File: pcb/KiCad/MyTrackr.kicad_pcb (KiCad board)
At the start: 2 copper layers, 50 x 50 mm, 37 parts, among them CN1 ANT, CON1 MICRO_SD, P1 OLED, P2 ICSP, P3 CONN_01X05, P4 CONN_BAT, Q1 Q_PMOS_GSD, SW1 RESET, SW2 SEL, SW3 NEXT, SW4 PREV, SW5 BACK, U0 10A45B_Module, U1 ATMEGA48_88_168_328P-32SMD, U2 GPS-NEO-6M, U3 24AA32

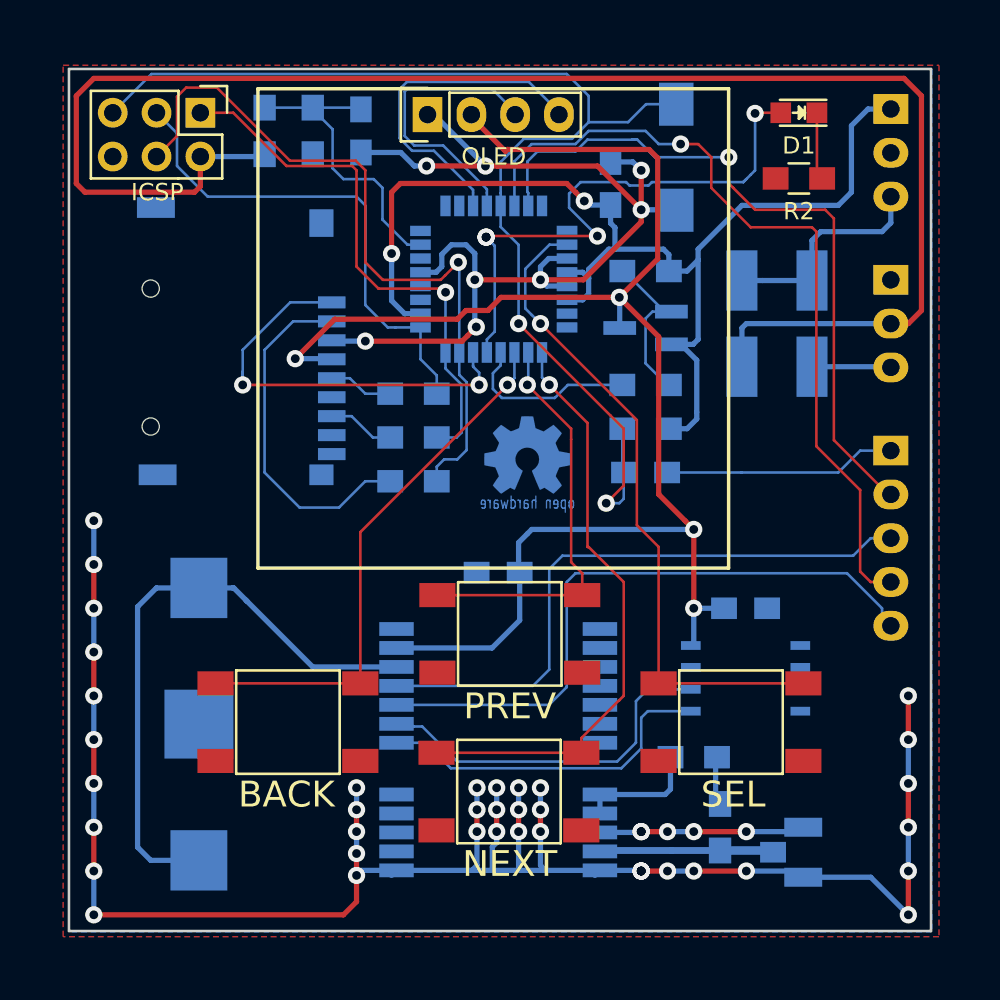
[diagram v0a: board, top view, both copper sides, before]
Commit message: Corrections and tweaks after first prototype
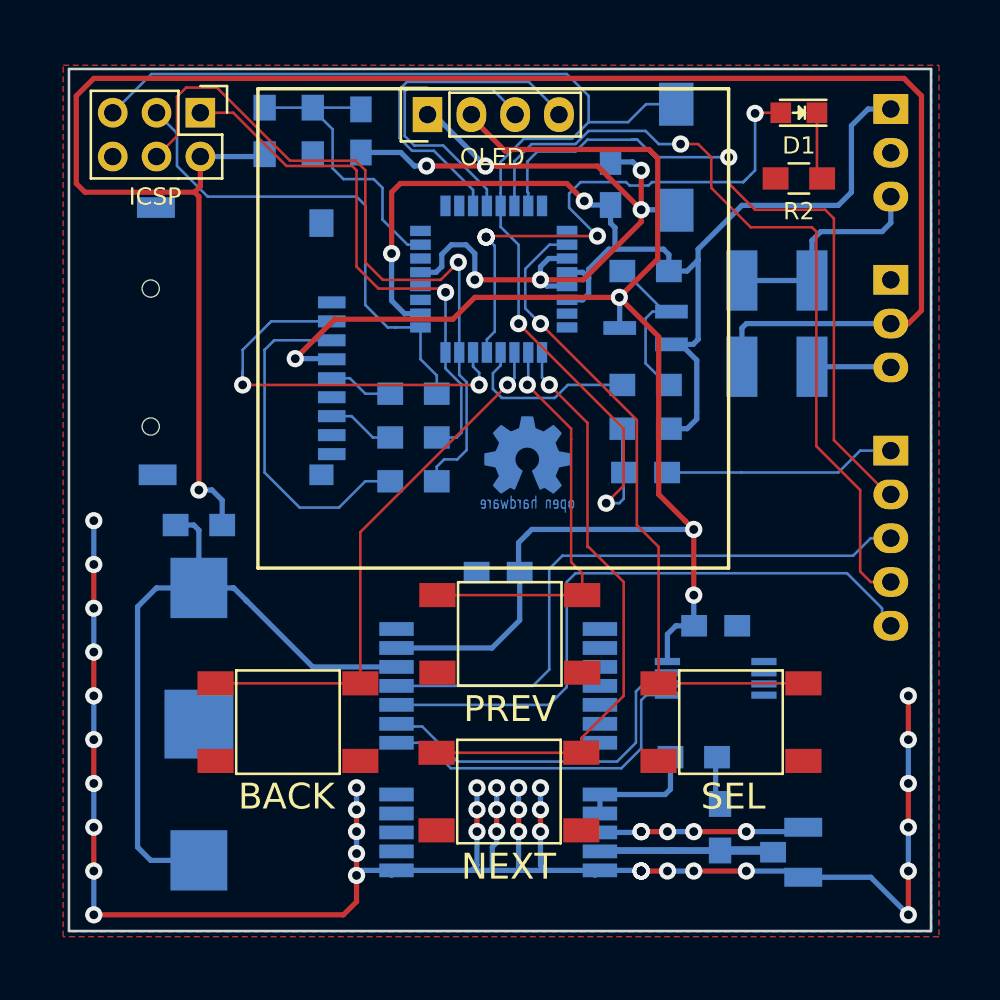
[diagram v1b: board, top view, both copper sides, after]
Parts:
- added JP1: NO, Resistors_SMD:R_0805_HandSoldering, B.Cu at (97.5, 76.5)
- BT2: value BAT -> GPS_BKP
- CN1: value ANT -> GPS_ANTENNA
- J2: renamed from P2; value ICSP -> CONN_ICSP
- P1: value OLED -> CONN_OLED
- R6, R7, R8: value 100 -> 1k
- SW1: value RESET -> BTN_RESET
- SW2: value SEL -> BTN_SEL
- SW3: value NEXT -> BTN_NEXT
- SW4: value PREV -> BTN_PREV
- SW5: value BACK -> BTN_BACK
- U2: footprint Sukko:NEO-6M -> MOUDLE-GPS-NEO-6M_24P-16X12.2MM_:GPS24P-SMD-1.1-16X12.2MM
- U3: footprint SparkFun-Footprints:SF-SOIC-8 -> w_smd_dil:tssop-8
- moved C4 2.01 mm to (127.5, 82.3)
- moved U3 1.73 mm to (127.5, 85.3)
- renumbered U0 to J1, P3 to J3, P4 to J4
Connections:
- CON1 pad 1: /CS -> (no net)
- CON1 pad 2: /DATA_IN -> /CS
- CON1 pad 3: GND -> /DATA_IN
- D1 pad 2: /ARDUINO_PIN_8 -> /ARDUINO_PIN_9
- R10 pad 1: /ARDUINO_PIN_9 -> /ARDUINO_PIN_8
- U1 pad 12: /ARDUINO_PIN_9 -> /ARDUINO_PIN_8
- U1 pad 13: /ARDUINO_PIN_8 -> /ARDUINO_PIN_9
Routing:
- net /ARDUINO_PIN_9: track 10.3 -> 33.3 mm, vias 0 -> 4
- net /ARDUINO_PIN_8: track 33.3 -> 10.3 mm, vias 4 -> 0
- net /VBAT: track 93.5 -> 113.9 mm, vias 0 -> 1
- net GND: track 185.3 -> 173.8 mm, vias 53 -> 51
- net Net-(BT2-Pad1): track 35.0 -> 39.9 mm
- net Net-(U2-Pad19): track 21.1 -> 20.2 mm
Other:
- net class Power: clearance 0.3048 -> 0.1524
- rule trace_min: 0.01 -> 0.1524
- board text added: "ANT"
- board text added: "BACK"
- board text added: "BAT"
- board text added: "ICSP"
- board text added: "NEXT"
- board text added: "OLED"
- board text added: "PREV"
- board text added: "RESET"
- board text added: "SEL"
- board text added: "V1.1"
- board text added: "Vi"
- board text added: "Vo"
- board text removed: "V1.0"

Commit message: Expand zones
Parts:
- moved G*** 0.25 mm to (116.3, 72.4)
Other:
- rule pad_to_mask_clearance: 0.2 -> 0
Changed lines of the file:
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@@
     (thickness 1.6)
     (drawings 39)
-    (tracks 589)
+    (tracks 586)
     (zones 0)
     (modules 38)
@@
     (last_trace_width 0.1524)
     (trace_clearance 0.1524)
-    (zone_clearance 0.2)
+    (zone_clearance 0.1524)
     (zone_45_only no)
     (trace_min 0.1524)
@@
     (mod_text_size 1 1)
     (mod_text_width 0.15)
-    (pad_size 2.032 1.7272)
-    (pad_drill 1.016)
-    (pad_to_mask_clearance 0.2)
+    (pad_size 2 0.8)
+    (pad_drill 0)
+    (pad_to_mask_clearance 0)
     (aux_axis_origin 0 0)
     (visible_elements FFFFFF7F)
@@
   (module MOUDLE-GPS-NEO-6M_24P-16X12.2MM_:GPS24P-SMD-1.1-16X12.2MM (layer B.Cu)
     (at 114.892 89.37 180)
-    (solder_mask_margin 0.1)
     (attr smd)
     (fp_text reference U2 (at -6.266 9.614 180) (layer B.SilkS)
       (effects (font (size 1 1) (thickness 0.15)) (justify mirror))
     )
-    (fp_text value GPS-NEO-6M (at 3.81 10.16 180) (layer B.SilkS) hide
+    (fp_text value GPS-NEO-6M (at 0 -1.27 180) (layer B.SilkS) hide
       (effects (font (size 1 1) (thickness 0.05)) (justify mirror))
     )
@@
     (fp_circle (center -6.985 8.255) (end -6.731 8.255) (layer B.SilkS) (width 0.508))
     (pad 1 smd rect (at -5.904 6.888) (size 2 0.8) (layers B.Cu B.Mask)
-      (solder_mask_margin 0.2))
+      (clearance 0.2))
     (pad 2 smd rect (at -5.904 5.788) (size 2 0.8) (layers B.Cu B.Mask)
-      (solder_mask_margin 0.2))
+      (clearance 0.2))
     (pad 3 smd rect (at -5.904 4.688) (size 2 0.8) (layers B.Cu B.Mask)
-      (solder_mask_margin 0.2))
+      (clearance 0.2))
     (pad 4 smd rect (at -5.904 3.588) (size 2 0.8) (layers B.Cu B.Mask)
-      (solder_mask_margin 0.2))
+      (clearance 0.2))
     (pad 5 smd rect (at -5.904 2.488) (size 2 0.8) (layers B.Cu B.Mask)
-      (solder_mask_margin 0.2))
+      (clearance 0.2))
     (pad 6 smd rect (at -5.904 1.388) (size 2 0.8) (layers B.Cu B.Mask)
-      (solder_mask_margin 0.2))
+      (clearance 0.2))
     (pad 7 smd rect (at -5.904 0.288) (size 2 0.8) (layers B.Cu B.Mask)
-      (net 2 GND) (solder_mask_margin 0.2))
+      (net 2 GND) (clearance 0.2))
     (pad 8 smd rect (at -5.904 -2.712) (size 2 0.8) (layers B.Cu B.Mask)
-      (net 25 "Net-(R3-Pad2)") (solder_mask_margin 0.2))
+      (net 25 "Net-(R3-Pad2)") (clearance 0.2))
     (pad 9 smd rect (at -5.904 -3.812) (size 2 0.8) (layers B.Cu B.Mask)
-      (net 25 "Net-(R3-Pad2)") (solder_mask_margin 0.2))
+      (net 25 "Net-(R3-Pad2)") (clearance 0.2))
     (pad 10 smd rect (at -5.904 -4.912) (size 2 0.8) (layers B.Cu B.Mask)
-      (net 2 GND) (solder_mask_margin 0.2))
+      (net 2 GND) (clearance 0.2))
     (pad 11 smd rect (at -5.904 -6.012) (size 2 0.8) (layers B.Cu B.Mask)
-      (net 13 "Net-(CN1-Pad1)") (solder_mask_margin 0.2))
+      (net 13 "Net-(CN1-Pad1)") (clearance 0.2))
     (pad 12 smd rect (at -5.904 -7.112) (size 2 0.8) (layers B.Cu B.Mask)
-      (net 2 GND) (solder_mask_margin 0.2))
+      (net 2 GND) (clearance 0.2))
     (pad 13 smd rect (at 5.896 -7.112) (size 2 0.8) (layers B.Cu B.Mask)
-      (net 2 GND) (solder_mask_margin 0.2))
+      (net 2 GND) (clearance 0.2))
     (pad 14 smd rect (at 5.896 -6.012) (size 2 0.8) (layers B.Cu B.Mask)
-      (solder_mask_margin 0.2))
+      (clearance 0.2))
     (pad 15 smd rect (at 5.896 -4.912) (size 2 0.8) (layers B.Cu B.Mask)
-      (solder_mask_margin 0.2))
+      (clearance 0.2))
     (pad 16 smd rect (at 5.896 -3.812) (size 2 0.8) (layers B.Cu B.Mask)
-      (solder_mask_margin 0.2))
+      (clearance 0.2))
     (pad 17 smd rect (at 5.896 -2.712) (size 2 0.8) (layers B.Cu B.Mask)
-      (solder_mask_margin 0.2))
+      (clearance 0.2))
     (pad 18 smd rect (at 5.896 0.288) (size 2 0.8) (layers B.Cu B.Mask)
-      (net 26 "Net-(U2-Pad18)") (solder_mask_margin 0.2))
+      (net 26 "Net-(U2-Pad18)") (clearance 0.2))
     (pad 19 smd rect (at 5.896 1.388) (size 2 0.8) (layers B.Cu B.Mask)
-      (net 27 "Net-(U2-Pad19)") (solder_mask_margin 0.2))
+      (net 27 "Net-(U2-Pad19)") (clearance 0.2))
     (pad 20 smd rect (at 5.896 2.488) (size 2 0.8) (layers B.Cu B.Mask)
-      (net 23 /GPS_TX) (solder_mask_margin 0.2))
+      (net 23 /GPS_TX))
     (pad 21 smd rect (at 5.896 3.588) (size 2 0.8) (layers B.Cu B.Mask)
-      (net 24 /GPS_RX) (solder_mask_margin 0.2))
+      (net 24 /GPS_RX) (clearance 0.2))
     (pad 22 smd rect (at 5.896 4.688) (size 2 0.8) (layers B.Cu B.Mask)
-      (net 22 "Net-(BT2-Pad1)") (solder_mask_margin 0.2))
+      (net 22 "Net-(BT2-Pad1)") (clearance 0.2))
     (pad 23 smd rect (at 5.896 5.788) (size 2 0.8) (layers B.Cu B.Mask)
-      (net 33 VPP) (solder_mask_margin 0.2))
+      (net 33 VPP) (clearance 0.2))
     (pad 24 smd rect (at 5.896 6.888) (size 2 0.8) (layers B.Cu B.Mask)
-      (net 2 GND) (solder_mask_margin 0.2))
+      (net 2 GND) (clearance 0.2))
   )
   (module MyKiCadLibs-Footprints:SW_TACT_SMD (layer F.Cu)
@@
   )
   (module w_logo:Logo_copper_OSHW_6x6mm (layer B.Cu)
-    (at 116.586 72.39 180)
+    (at 116.332 72.39 180)
     (descr "Open Hardware Logo, 6x6mm")
     (fp_text reference G*** (at 0 0 180) (layer B.SilkS) hide
@@
   (segment (start 129.286 64.77) (end 129.032 65.024) (width 0.3048) (layer B.Cu) (net 1))
   (segment (start 129.032 65.024) (end 129.032 67.26936) (width 0.3048) (layer B.Cu) (net 1))
+  (segment (start 123.19 55.626) (end 123.19 58.166) (width 0.3048) (layer F.Cu) (net 2))
+  (segment (start 121.412 55.392) (end 122.956 55.392) (width 0.3048) (layer B.Cu) (net 2))
+  (segment (start 122.956 55.392) (end 123.19 55.626) (width 0.3048) (layer B.Cu) (net 2))
+  (via (at 123.19 55.626) (size 1) (drill 0.508) (layers F.Cu B.Cu) (net 2))
   (segment (start 116.078 92.964) (end 116.078 91.694) (width 0.3048) (layer B.Cu) (net 2))
   (via (at 116.078 91.694) (size 1) (drill 0.508) (layers F.Cu B.Cu) (net 2))
@@
   (segment (start 113.03 60.198) (end 113.538 60.706) (width 0.3048) (layer B.Cu) (net 2))
   (segment (start 113.538 60.706) (end 113.538 62.23) (width 0.3048) (layer B.Cu) (net 2))
-  (segment (start 123.19 55.88) (end 123.19 58.166) (width 0.3048) (layer F.Cu) (net 2))
-  (segment (start 122.702 55.392) (end 123.19 55.88) (width 0.3048) (layer B.Cu) (net 2))
-  (segment (start 121.412 55.392) (end 122.702 55.392) (width 0.3048) (layer B.Cu) (net 2))
-  (via (at 123.19 55.88) (size 1) (drill 0.508) (layers F.Cu B.Cu) (net 2))
   (segment (start 110.744 55.626) (end 114.15137 55.626) (width 0.3048) (layer F.Cu) (net 2))
   (segment (start 114.15137 55.626) (end 114.15699 55.63162) (width 0.3048) (layer F.Cu) (net 2))
@@
   (segment (start 137.5156 74.676) (end 137.668 74.676) (width 0.1524) (layer F.Cu) (net 18))
   (segment (start 122.682 54.102) (end 122.936 54.102) (width 0.1524) (layer B.Cu) (net 18))
+  (segment (start 120.65 59.69) (end 119.006998 58.046998) (width 0.1524) (layer B.Cu) (net 19))
+  (segment (start 119.006998 58.046998) (end 119.006998 57.235118) (width 0.1524) (layer B.Cu) (net 19))
+  (segment (start 119.006998 57.235118) (end 119.680117 56.561999) (width 0.1524) (layer B.Cu) (net 19))
+  (segment (start 119.680117 56.561999) (end 123.811885 56.561999) (width 0.1524) (layer B.Cu) (net 19))
+  (segment (start 123.811885 56.561999) (end 129.112001 56.561999) (width 0.1524) (layer B.Cu) (net 19))
   (segment (start 129.794 52.578) (end 129.794 55.88) (width 0.1524) (layer B.Cu) (net 19))
   (segment (start 129.794 55.88) (end 129.54 56.134) (width 0.1524) (layer B.Cu) (net 19))
@@
   (segment (start 114.238 65.6896) (end 114.694193 65.233407) (width 0.1524) (layer B.Cu) (net 19))
   (segment (start 114.694193 65.233407) (end 114.694193 60.254493) (width 0.1524) (layer B.Cu) (net 19))
-  (segment (start 122.513118 56.761002) (end 123.612882 56.761002) (width 0.1524) (layer B.Cu) (net 19))
-  (segment (start 122.314115 56.561999) (end 122.513118 56.761002) (width 0.1524) (layer B.Cu) (net 19))
-  (segment (start 120.65 59.69) (end 119.006998 58.046998) (width 0.1524) (layer B.Cu) (net 19))
-  (segment (start 123.811885 56.561999) (end 129.112001 56.561999) (width 0.1524) (layer B.Cu) (net 19))
-  (segment (start 119.680117 56.561999) (end 122.314115 56.561999) (width 0.1524) (layer B.Cu) (net 19))
-  (segment (start 119.006998 57.235118) (end 119.680117 56.561999) (width 0.1524) (layer B.Cu) (net 19))
-  (segment (start 123.612882 56.761002) (end 123.811885 56.561999) (width 0.1524) (layer B.Cu) (net 19))
-  (segment (start 119.006998 58.046998) (end 119.006998 57.235118) (width 0.1524) (layer B.Cu) (net 19))
   (via (at 120.65 59.69) (size 1) (drill 0.508) (layers F.Cu B.Cu) (net 19))
   (segment (start 129.112001 56.561999) (end 129.54 56.134) (width 0.1524) (layer B.Cu) (net 19))
@@
   (segment (start 123.8416 64.074) (end 124.944 64.074) (width 0.1524) (layer B.Cu) (net 36))
   (zone (net 2) (net_name GND) (layer F.Cu) (hatch edge 0.508)
-    (connect_pads (clearance 0.2))
-    (min_thickness 0.1)
-    (fill (arc_segments 16) (thermal_gap 0.508) (thermal_bridge_width 0.508))
+    (connect_pads (clearance 0.1524))
+    (min_thickness 0.0254)
+    (fill yes (arc_segments 16) (thermal_gap 0.1524) (thermal_bridge_width 0.254))
     (polygon
       (pts
@@
   )
   (zone (net 2) (net_name GND) (layer B.Cu) (hatch edge 0.508)
-    (connect_pads (clearance 0.2))
-    (min_thickness 0.1)
-    (fill (arc_segments 16) (thermal_gap 0.508) (thermal_bridge_width 0.508))
+    (connect_pads (clearance 0.1524))
+    (min_thickness 0.0254)
+    (fill yes (arc_segments 16) (thermal_gap 0.1524) (thermal_bridge_width 0.254))
     (polygon
       (pts
